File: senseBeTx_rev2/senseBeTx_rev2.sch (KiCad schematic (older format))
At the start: 37 parts

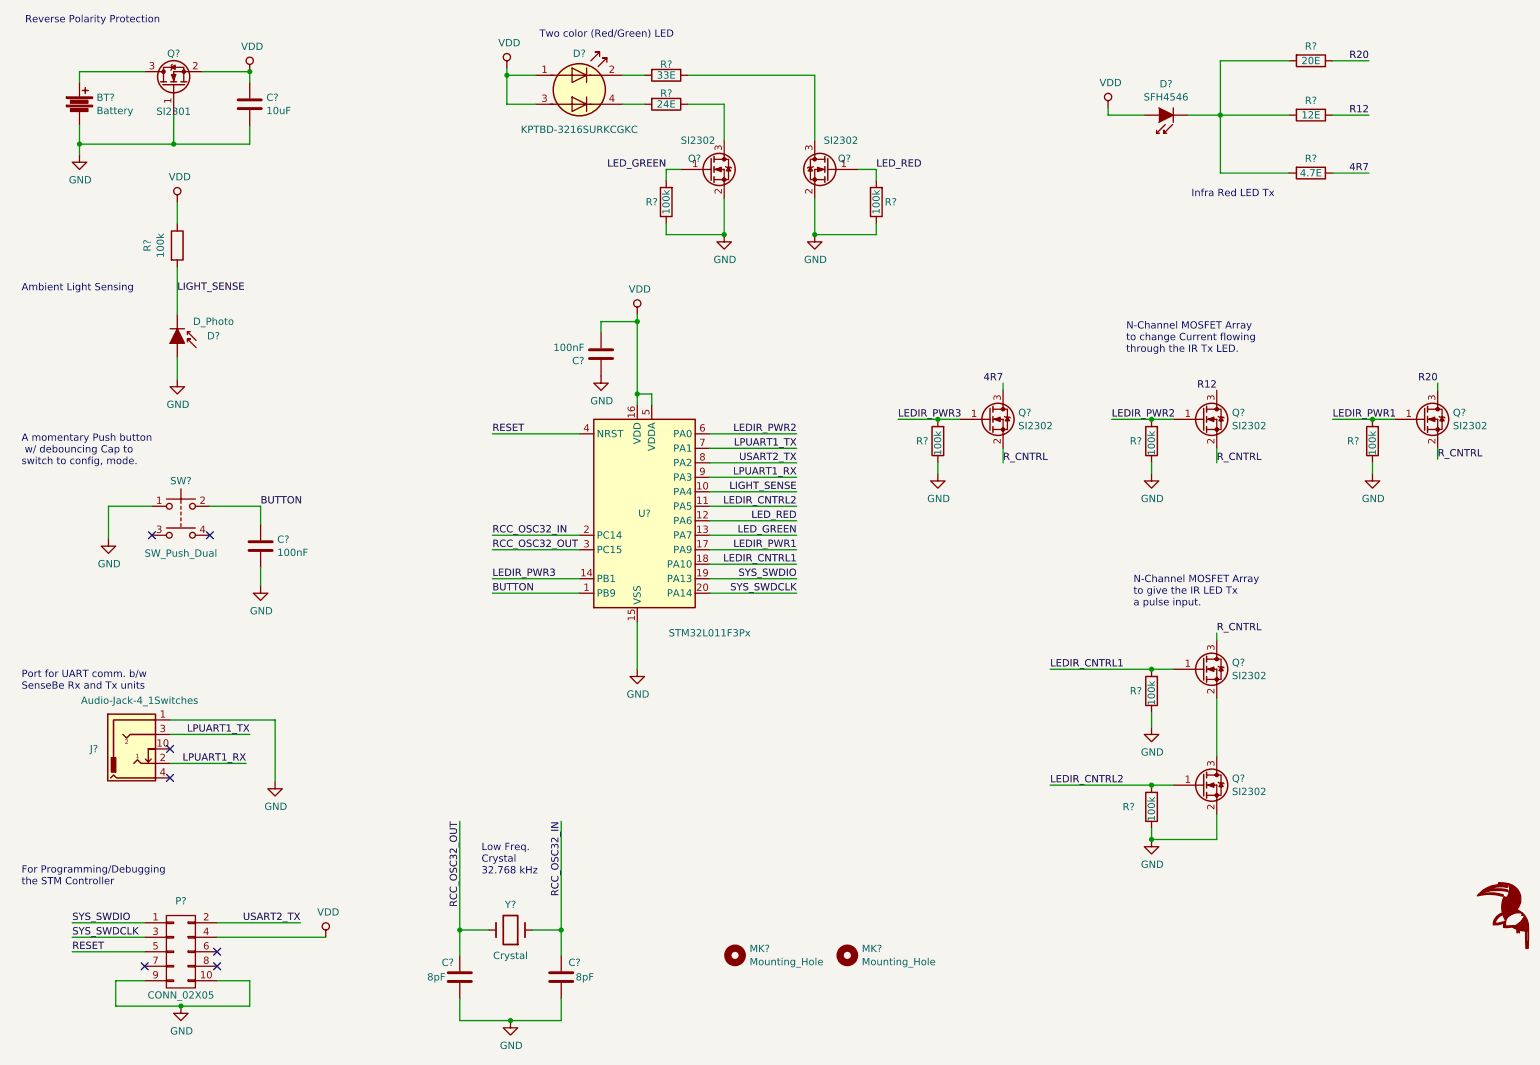
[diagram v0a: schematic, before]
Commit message: Adds Schematic and PCB Files of SenseBe rev2
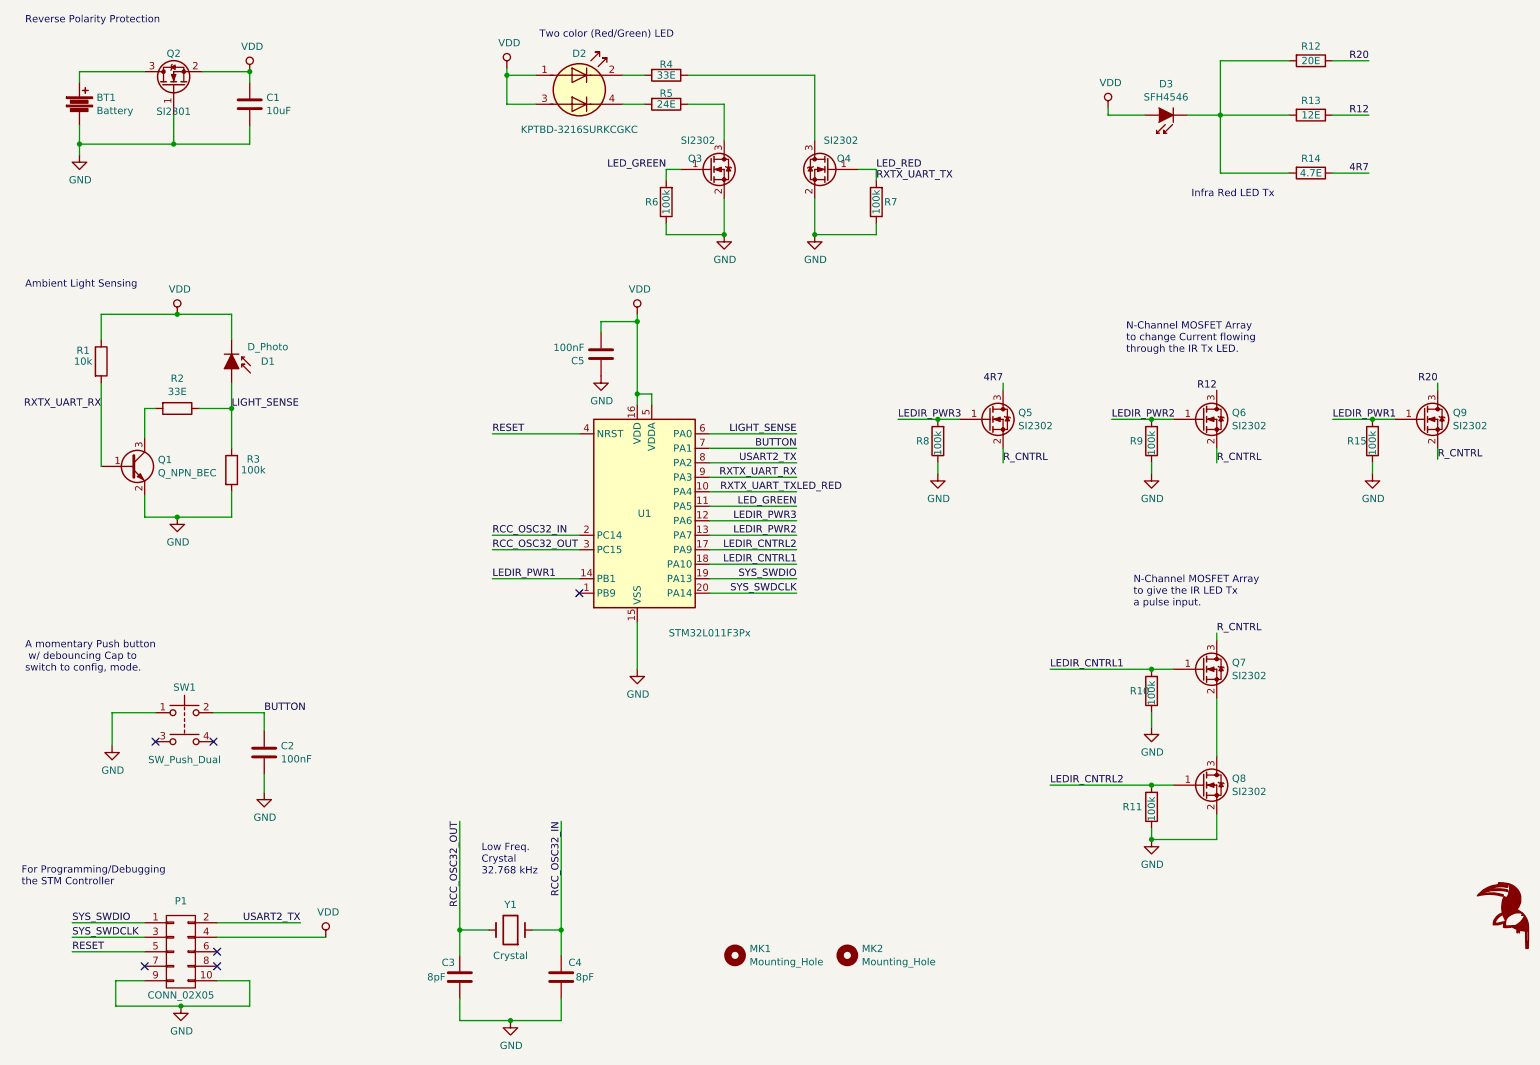
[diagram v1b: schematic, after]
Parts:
- removed J?: Audio-Jack-4_1Switches, senseBeTx_rev1_fp:SJ2-35863B1-SMT, symbol senseBeRx_rev1:Audio-Jack-4_1Switches
- added Q1: Q_NPN_BEC, Package_TO_SOT_SMD:SOT-23, symbol Device:Q_NPN_BEC
- added R2: 33E, Resistor_SMD:R_0603_1608Metric_Pad1.05x0.95mm_HandSolder, symbol senseBeRx_rev1:R
- added R3: 100k, Resistor_SMD:R_0603_1608Metric_Pad1.05x0.95mm_HandSolder, symbol senseBeRx_rev1:R
- R1: renamed from R?; value 100k -> 10k
- gave numbers to parts that had none: 35
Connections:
- net LPUART1_TX is gone; now on net BUTTON: U1.7 (PA1)
- net BUTTON: no longer U1.1 (PB9)
- net GND: now also Q1.2 (E), R3.2; no longer D1.2 (A)
- net LEDIR_CNTRL2: now also U1.17 (PA9); no longer U1.11 (PA5)
- net LEDIR_PWR1: now also U1.14 (PB1); no longer U1.17 (PA9)
- net LEDIR_PWR2: now also U1.13 (PA7); no longer U1.6 (PA0)
- net LEDIR_PWR3: now also U1.12 (PA6); no longer U1.14 (PB1)
- net LED_GREEN: now also U1.11 (PA5); no longer U1.13 (PA7)
- net LED_RED: now also U1.10 (PA4); no longer U1.12 (PA6)
- net LIGHT_SENSE: now also D1.2 (A), U1.6 (PA0), R2.1, R3.1; no longer D1.1 (K), R1.2, U1.10 (PA4)
- net VDD: now also D1.1 (K)
- net LPUART1_RX renamed RXTX_UART_RX
- net RXTX_UART_RX: now also R1.2, Q1.1 (B)
- new net: Q1.3 (C), R2.2
- no-connect marks 7 -> 6
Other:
- note removed: "Port for UART comm. b/w \nSenseBe Rx and Tx units"
- moved on the sheet: C2, D1, R1, SW1

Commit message: Adds all SenseBe_RX and _TX updated PCB, Schematic and Gerber files
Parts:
- MK1, MK2: footprint senseBeTx_rev1_fp:MountingHole_3.2mm_M3 -> MountingHole:MountingHole_3.2mm_M3
- Q1: value Q_NPN_BEC -> BC847
- Q9: footprint senseBeTx_rev1_fp:SOT-23 -> senseBeTx_rev2_fp:SOT-23
- R12: value 20E -> 56E
- R13: value 12E -> 20E
- R14: value 4.7E -> 2.7E
- SW1: footprint Button_Switch_THT:SW_TH_Tactile_Omron_B3F-10xx -> Button_Switch_THT:SW_PUSH_6mm; symbol senseBeRx_rev1:SW_Push_Dual -> Switch:SW_SPST
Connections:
- net R12 is gone; now on net R20: Q6.3 (D), R13.1
- net GND: now also U1.1 (PB9)
- net R20: no longer Q9.3 (D), R12.1
- net RXTX_UART_RX: now also Q1.3 (C); no longer Q1.1 (B)
- net at R2.2: now also Q1.1 (B); no longer Q1.3 (C)
- net 4R7 renamed 2R7
- new net R56: Q9.3 (D), R12.1
- no-connect marks 6 -> 3
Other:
- moved on the sheet: Q1
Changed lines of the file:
@@
 F 0 "MK2" H 6350 7146 50  0000 L CNN
 F 1 "Mounting_Hole" H 6350 7055 50  0000 L CNN
-F 2 "senseBeTx_rev1_fp:MountingHole_3.2mm_M3" H 6250 7100 50  0001 C CNN
+F 2 "MountingHole:MountingHole_3.2mm_M3" H 6250 7100 50  0001 C CNN
 F 3 "" H 6250 7100 50  0001 C CNN
 	1    6250 7100
-	1    0    0    -1
-$EndComp
-$Comp
-L Device:Q_NMOS_GSD Q9
-U 1 1 5BB214EE
-P 10225 3400
-F 0 "Q9" H 10430 3446 50  0000 L CNN
-F 1 "SI2302" H 10430 3355 50  0000 L CNN
-F 2 "senseBeTx_rev1_fp:SOT-23" H 10425 3500 50  0001 C CNN
-F 3 "~" H 10225 3400 50  0001 C CNN
-	1    10225 3400
 	1    0    0    -1
 $EndComp
@@
 $EndComp
 $Comp
-L senseBeRx_rev1:SW_Push_Dual SW1
+L Switch:SW_SPST SW1
 U 1 1 5BB21947
 P 1675 5425
 F 0 "SW1" H 1675 5600 50  0000 C CNN
-F 1 "SW_Push_Dual" H 1675 5100 50  0000 C CNN
-F 2 "Button_Switch_THT:SW_TH_Tactile_Omron_B3F-10xx" H 1675 5625 50  0001 C CNN
+F 1 "SW_Push_Dual" H 1675 5250 50  0000 C CNN
+F 2 "Button_Switch_THT:SW_PUSH_6mm" H 1675 5625 50  0001 C CNN
 F 3 "" H 1675 5625 50  0001 C CNN
 	1    1675 5425
@@
 P 9450 925
 F 0 "R12" V 9350 925 50  0000 C CNN
-F 1 "20E" V 9450 925 50  0000 C CNN
+F 1 "56E" V 9450 925 50  0000 C CNN
 F 2 "Resistor_SMD:R_0603_1608Metric_Pad1.05x0.95mm_HandSolder" V 9380 925 30  0001 C CNN
 F 3 "" H 9450 925 30  0000 C CNN
@@
 P 9450 1300
 F 0 "R13" V 9350 1300 50  0000 C CNN
-F 1 "12E" V 9450 1300 50  0000 C CNN
+F 1 " 20E" V 9450 1275 50  0000 C CNN
 F 2 "Resistor_SMD:R_0603_1608Metric_Pad1.05x0.95mm_HandSolder" V 9380 1300 30  0001 C CNN
 F 3 "" H 9450 1300 30  0000 C CNN
@@
 P 9450 1700
 F 0 "R14" V 9350 1700 50  0000 C CNN
-F 1 "4.7E" V 9450 1700 50  0000 C CNN
+F 1 "2.7E" V 9450 1700 50  0000 C CNN
 F 2 "Resistor_SMD:R_0603_1608Metric_Pad1.05x0.95mm_HandSolder" V 9380 1700 30  0001 C CNN
 F 3 "" H 9450 1700 30  0000 C CNN
@@
 U 1 1 5BB2589F
 P 9875 3550
-F 0 "R15" H 10050 3550 50  0000 R CNN
+F 0 "R15" H 10075 3550 50  0000 R CNN
 F 1 "100k" V 9875 3650 50  0000 R CNN
 F 2 "Resistor_SMD:R_0603_1608Metric_Pad1.05x0.95mm_HandSolder" V 9805 3550 30  0001 C CNN
@@
 U 1 1 5BB25C33
 P 8350 5275
-F 0 "R10" H 8500 5275 50  0000 R CNN
+F 0 "R10" H 8550 5275 50  0000 R CNN
 F 1 "100k" V 8350 5375 50  0000 R CNN
 F 2 "Resistor_SMD:R_0603_1608Metric_Pad1.05x0.95mm_HandSolder" V 8280 5275 30  0001 C CNN
@@
 	1600 1500 950  1500
 $Comp
-L senseBeRx_rev1:VDD #PWR017
+L senseBeRx_rev1:VDD #PWR018
 U 1 1 5BB27ED8
 P 8050 1250
-F 0 "#PWR017" H 8050 1100 50  0001 C CNN
+F 0 "#PWR018" H 8050 1100 50  0001 C CNN
 F 1 "VDD" H 8067 1423 50  0000 C CNN
 F 2 "" H 8050 1250 60  0000 C CNN
@@
 	7325 3150 7325 3200
 $Comp
-L senseBeRx_rev1:GND #PWR014
+L senseBeRx_rev1:GND #PWR015
 U 1 1 5BB2949E
 P 5400 2125
-F 0 "#PWR014" H 5400 1875 50  0001 C CNN
+F 0 "#PWR015" H 5400 1875 50  0001 C CNN
 F 1 "GND" H 5405 1952 50  0000 C CNN
 F 2 "" H 5400 2125 60  0000 C CNN
@@
 $EndComp
 $Comp
-L senseBeRx_rev1:GND #PWR021
+L senseBeRx_rev1:GND #PWR022
 U 1 1 5BB297D5
 P 9875 3775
-F 0 "#PWR021" H 9875 3525 50  0001 C CNN
+F 0 "#PWR022" H 9875 3525 50  0001 C CNN
 F 1 "GND" H 9880 3602 50  0000 C CNN
 F 2 "" H 9875 3775 60  0000 C CNN
@@
 $EndComp
 $Comp
-L senseBeRx_rev1:GND #PWR018
+L senseBeRx_rev1:GND #PWR019
 U 1 1 5BB29993
 P 8350 3775
-F 0 "#PWR018" H 8350 3525 50  0001 C CNN
+F 0 "#PWR019" H 8350 3525 50  0001 C CNN
 F 1 "GND" H 8355 3602 50  0000 C CNN
 F 2 "" H 8350 3775 60  0000 C CNN
@@
 $EndComp
 $Comp
-L senseBeRx_rev1:GND #PWR016
+L senseBeRx_rev1:GND #PWR017
 U 1 1 5BB29AC0
 P 6875 3775
-F 0 "#PWR016" H 6875 3525 50  0001 C CNN
+F 0 "#PWR017" H 6875 3525 50  0001 C CNN
 F 1 "GND" H 6880 3602 50  0000 C CNN
 F 2 "" H 6875 3775 60  0000 C CNN
@@
 $EndComp
 $Comp
-L senseBeRx_rev1:GND #PWR019
+L senseBeRx_rev1:GND #PWR020
 U 1 1 5BB29EDA
 P 8350 5525
-F 0 "#PWR019" H 8350 5275 50  0001 C CNN
+F 0 "#PWR020" H 8350 5275 50  0001 C CNN
 F 1 "GND" H 8355 5352 50  0000 C CNN
 F 2 "" H 8350 5525 60  0000 C CNN
@@
 $EndComp
 $Comp
-L senseBeRx_rev1:GND #PWR020
+L senseBeRx_rev1:GND #PWR021
 U 1 1 5BB29F1F
 P 8350 6300
-F 0 "#PWR020" H 8350 6050 50  0001 C CNN
+F 0 "#PWR021" H 8350 6050 50  0001 C CNN
 F 1 "GND" H 8355 6127 50  0000 C CNN
 F 2 "" H 8350 6300 60  0000 C CNN
@@
 $EndComp
 $Comp
-L senseBeRx_rev1:GND #PWR015
+L senseBeRx_rev1:GND #PWR016
 U 1 1 5BB4CBB1
 P 6025 2125
-F 0 "#PWR015" H 6025 1875 50  0001 C CNN
+F 0 "#PWR016" H 6025 1875 50  0001 C CNN
 F 1 "GND" H 6030 1952 50  0000 C CNN
 F 2 "" H 6025 2125 60  0000 C CNN
@@
 $EndComp
 $Comp
-L senseBeRx_rev1:VDD #PWR09
+L senseBeRx_rev1:VDD #PWR010
 U 1 1 5BB4CD6E
 P 3900 975
-F 0 "#PWR09" H 3900 825 50  0001 C CNN
+F 0 "#PWR010" H 3900 825 50  0001 C CNN
 F 1 "VDD" H 3917 1148 50  0000 C CNN
 F 2 "" H 3900 975 60  0000 C CNN
@@
 Wire Wire Line
 	6025 1025 6025 1475
-NoConn ~ 1475 5625
-NoConn ~ 1875 5625
 $Comp
 L senseBeRx_rev1:Mounting_Hole MK1
@@
 F 0 "MK1" H 5575 7146 50  0000 L CNN
 F 1 "Mounting_Hole" H 5575 7055 50  0000 L CNN
-F 2 "senseBeTx_rev1_fp:MountingHole_3.2mm_M3" H 5475 7100 50  0001 C CNN
+F 2 "MountingHole:MountingHole_3.2mm_M3" H 5475 7100 50  0001 C CNN
 F 3 "" H 5475 7100 50  0001 C CNN
 	1    5475 7100
@@
 $EndComp
 $Comp
-L senseBeRx_rev1:GND #PWR010
+L senseBeRx_rev1:GND #PWR011
 U 1 1 5BB5CD23
 P 3925 7550
-F 0 "#PWR010" H 3925 7300 50  0001 C CNN
+F 0 "#PWR011" H 3925 7300 50  0001 C CNN
 F 1 "GND" H 3930 7377 50  0000 C CNN
 F 2 "" H 3925 7550 60  0000 C CNN
@@
 L senseBeRx_rev1:GND #PWR04
 U 1 1 5BC0B655
-P 1625 4075
-F 0 "#PWR04" H 1625 3825 50  0001 C CNN
-F 1 "GND" H 1630 3902 50  0000 C CNN
-F 2 "" H 1625 4075 60  0000 C CNN
-F 3 "" H 1625 4075 60  0000 C CNN
-	1    1625 4075
+P 1575 4100
+F 0 "#PWR04" H 1575 3850 50  0001 C CNN
+F 1 "GND" H 1580 3927 50  0000 C CNN
+F 2 "" H 1575 4100 60  0000 C CNN
+F 3 "" H 1575 4100 60  0000 C CNN
+	1    1575 4100
 	1    0    0    -1
 $EndComp
@@
 L senseBeRx_rev1:VDD #PWR03
 U 1 1 5BC0BA50
-P 1625 2675
-F 0 "#PWR03" H 1625 2525 50  0001 C CNN
-F 1 "VDD" H 1642 2848 50  0000 C CNN
-F 2 "" H 1625 2675 60  0000 C CNN
-F 3 "" H 1625 2675 60  0000 C CNN
-	1    1625 2675
+P 1575 2600
+F 0 "#PWR03" H 1575 2450 50  0001 C CNN
+F 1 "VDD" H 1592 2773 50  0000 C CNN
+F 2 "" H 1575 2600 60  0000 C CNN
+F 3 "" H 1575 2600 60  0000 C CNN
+	1    1575 2600
 	1    0    0    -1
 $EndComp
@@
 LEDIR_PWR3
 $Comp
-L senseBeRx_rev1:VDD #PWR012
+L senseBeRx_rev1:VDD #PWR013
 U 1 1 5BC22F0C
 P 4800 2675
-F 0 "#PWR012" H 4800 2525 50  0001 C CNN
+F 0 "#PWR013" H 4800 2525 50  0001 C CNN
 F 1 "VDD" H 4817 2848 50  0000 C CNN
 F 2 "" H 4800 2675 60  0000 C CNN
@@
 	4800 3225 4800 3300
 $Comp
-L senseBeRx_rev1:GND #PWR013
+L senseBeRx_rev1:GND #PWR014
 U 1 1 5BC6E4AA
 P 4800 5125
-F 0 "#PWR013" H 4800 4875 50  0001 C CNN
+F 0 "#PWR014" H 4800 4875 50  0001 C CNN
 F 1 "GND" H 4805 4952 50  0000 C CNN
 F 2 "" H 4800 5125 60  0000 C CNN
@@
 	8825 925  8825 1300
 Text Label 9850 925  2    50   ~ 0
+R56
+Text Label 9850 1300 2    50   ~ 0
 R20
-Text Label 9850 1300 2    50   ~ 0
-R12
 Text Label 9850 1700 2    50   ~ 0
-4R7
+2R7
 Wire Wire Line
 	9850 1700 9600 1700
@@
 	9850 925  9600 925
 Text Label 10325 3150 2    50   ~ 0
+R56
+Text Label 8800 3150 2    50   ~ 0
 R20
-Text Label 8800 3200 2    50   ~ 0
-R12
 Text Label 7325 3150 2    50   ~ 0
-4R7
+2R7
 Wire Wire Line
 	10325 3150 10325 3200
@@
 $EndComp
 $Comp
-L senseBeRx_rev1:GND #PWR011
+L senseBeRx_rev1:GND #PWR012
 U 1 1 5BBB011A
 P 4550 3100
-F 0 "#PWR011" H 4550 2850 50  0001 C CNN
+F 0 "#PWR012" H 4550 2850 50  0001 C CNN
 F 1 "GND" H 4555 2927 50  0000 C CNN
 F 2 "" H 4550 3100 60  0000 C CNN
@@
 Text Label 5900 4100 2    50   ~ 0
 LEDIR_PWR3
-NoConn ~ 4400 4600
 Text Label 6450 1750 0    50   ~ 0
 RXTX_UART_TX
@@
 L Device:Q_NPN_BEC Q1
 U 1 1 5BFFF938
-P 1300 3725
-F 0 "Q1" H 1491 3771 50  0000 L CNN
-F 1 "Q_NPN_BEC" H 1491 3680 50  0000 L CNN
-F 2 "Package_TO_SOT_SMD:SOT-23" H 1500 3825 50  0001 C CNN
-F 3 "~" H 1300 3725 50  0001 C CNN
-	1    1300 3725
-	1    0    0    -1
+P 1200 3750
+F 0 "Q1" H 1391 3796 50  0000 L CNN
+F 1 "BC847" H 1391 3705 50  0000 L CNN
+F 2 "Package_TO_SOT_SMD:SOT-23" H 1400 3850 50  0001 C CNN
+F 3 "~" H 1200 3750 50  0001 C CNN
+	1    1200 3750
+	-1   0    0    -1
 $EndComp
 Wire Wire Line
 	1100 2850 1100 2675
 Wire Wire Line
-	1100 2675 1625 2675
-Wire Wire Line
-	1625 2675 2000 2675
-Wire Wire Line
 	2000 2675 2000 2850
-Connection ~ 1625 2675
 Wire Wire Line
 	1775 3325 2000 3325
@@
 	1475 3325 1400 3325
 Wire Wire Line
-	1400 3525 1400 3325
-Wire Wire Line
-	1400 3925 1400 4075
-Wire Wire Line
-	1400 4075 1625 4075
-Wire Wire Line
 	2000 3900 2000 4075
-Wire Wire Line
-	2000 4075 1625 4075
-Connection ~ 1625 4075
-Wire Wire Line
-	1100 3150 1100 3725
 Text Label 1100 3325 2    50   ~ 0
 RXTX_UART_RX
+Wire Wire Line
+	1100 3950 1100 4075
+Wire Wire Line
+	1400 3325 1400 3750
+Wire Wire Line
+	1100 3150 1100 3550
+Wire Wire Line
+	1100 4075 1575 4075
+Wire Wire Line
+	1575 4100 1575 4075
+Wire Wire Line
+	1100 2675 1575 2675
+Connection ~ 1575 4075
+Wire Wire Line
+	1575 4075 2000 4075
+Wire Wire Line
+	1575 2600 1575 2675
+Connection ~ 1575 2675
+Wire Wire Line
+	1575 2675 2000 2675
+$Comp
+L senseBeRx_rev1:GND #PWR09
+U 1 1 5C029F13
+P 3800 4650
+F 0 "#PWR09" H 3800 4400 50  0001 C CNN
+F 1 "GND" H 3805 4477 50  0000 C CNN
+F 2 "" H 3800 4650 60  0000 C CNN
+F 3 "" H 3800 4650 60  0000 C CNN
+	1    3800 4650
+	1    0    0    -1
+$EndComp
+Wire Wire Line
+	4400 4600 3800 4600
+Wire Wire Line
+	3800 4600 3800 4650
+$Comp
+L Device:Q_NMOS_GSD Q9
+U 1 1 5C03102F
+P 10225 3400
+F 0 "Q9" H 10430 3446 50  0000 L CNN
+F 1 "SI2302" H 10430 3355 50  0000 L CNN
+F 2 "senseBeTx_rev2_fp:SOT-23" H 10425 3500 50  0001 C CNN
+F 3 "~" H 10225 3400 50  0001 C CNN
+	1    10225 3400
+	1    0    0    -1
+$EndComp
+Wire Wire Line
+	8800 3150 8800 3200
 $EndSCHEMATC
